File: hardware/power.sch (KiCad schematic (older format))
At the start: 79 parts, among them J100 Conn_01x01, J101 Conn_01x01, J102 Conn_01x01, J39 Screw_Terminal_01x02, J44 Conn_01x01, J45 Conn_01x01, J48 Conn_01x01, J49 Conn_01x01, J50 Conn_01x01, J51 Conn_01x01, J53 Conn_01x01, J54 Conn_01x01, J55 Conn_01x01, J56 Conn_01x01, J57 Conn_01x01, J58 Conn_01x01, J59 Conn_01x01, J68 Conn_01x01, J69 Conn_01x01, J70 Conn_01x01, J94 Conn_01x01, J95 Conn_01x01, J96 Conn_01x01, J98 Conn_01x01, J99 Conn_01x01, Q1 AON6144, U2 LM1117-3.3

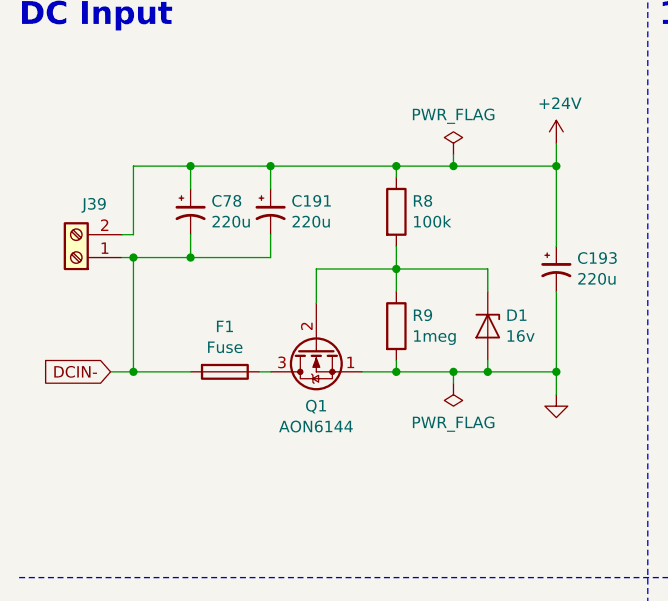
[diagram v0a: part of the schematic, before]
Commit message: replaced stepper driver
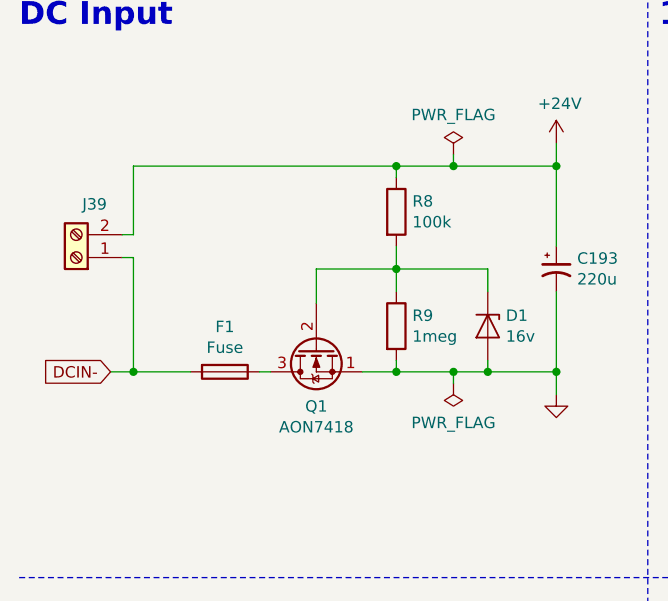
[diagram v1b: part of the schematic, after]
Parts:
- removed C191, C78: 220u, Capacitor_SMD:CP_Elec_6.3x7.7, symbol Device:CP1_Small
- Q1: value AON6144 -> AON7418
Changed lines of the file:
@@
 EESchema Schematic File Version 4
+LIBS:c3dpb-cache
 EELAYER 29 0
 EELAYER END
 $Descr A4 11693 8268
 encoding utf-8
-Sheet 2 10
+Sheet 2 8
 Title "Kajikia - Power Sheet"
 Date "2019-01-23"
@@
 U 1 1 5C3AA6BF
 P 1850 2150
-F 0 "Q1" V 2100 2150 50  0000 C CNN
-F 1 "AON6144" V 2191 2150 50  0000 C CNN
+F 0 "Q1" V 2101 2150 50  0000 C CNN
+F 1 "AON7418" V 2192 2150 50  0000 C CNN
 F 2 "_Generic:DFN5x6-8" H 2050 2250 50  0001 C CNN
 F 3 "~" H 1850 2150 50  0001 C CNN
@@
 	1050 2250 950  2250
 Connection ~ 1050 2250
-Wire Wire Line
-	1050 1350 1300 1350
 $Comp
 L Device:Fuse F1
@@
 	0    1    1    0
 $EndComp
-$Comp
-L Device:CP1_Small C78
-U 1 1 5C8D0CF9
-P 1300 1550
-F 0 "C78" H 1391 1596 50  0000 L CNN
-F 1 "220u" H 1391 1505 50  0000 L CNN
-F 2 "Capacitor_SMD:CP_Elec_6.3x7.7" H 1300 1550 50  0001 C CNN
-F 3 "~" H 1300 1550 50  0001 C CNN
-	1    1300 1550
-	1    0    0    -1
-$EndComp
-Wire Wire Line
-	1300 1650 1300 1750
 Wire Wire Line
 	1050 1750 1050 2250
-$Comp
-L Device:CP1_Small C191
-U 1 1 5C910F5C
-P 1650 1550
-F 0 "C191" H 1741 1596 50  0000 L CNN
-F 1 "220u" H 1741 1505 50  0000 L CNN
-F 2 "Capacitor_SMD:CP_Elec_6.3x7.7" H 1650 1550 50  0001 C CNN
-F 3 "~" H 1650 1550 50  0001 C CNN
-	1    1650 1550
-	1    0    0    -1
-$EndComp
-Wire Wire Line
-	1650 1650 1650 1750
-Wire Wire Line
-	1300 1750 1650 1750
-Connection ~ 1300 1750
 Wire Wire Line
 	1050 1350 1050 1650
-Wire Wire Line
-	1300 1350 1300 1450
-Connection ~ 1300 1350
-Wire Wire Line
-	1300 1350 1650 1350
-Wire Wire Line
-	1650 1350 1650 1450
-Connection ~ 1650 1350
-Wire Wire Line
-	1650 1350 2200 1350
 $Comp
 L Device:CP1_Small C193
@@
 Wire Notes Line
 	550  3150 10100 3150
-Connection ~ 1050 1750
-Wire Wire Line
-	1050 1750 1300 1750
 Wire Wire Line
 	1600 2250 1650 2250
@@
 Text Notes 4450 5350 0    50   ~ 0
 200k - 0.5mhz\n100k - 1mhz\n40k - 2.5mhz
+Wire Wire Line
+	1050 1350 2200 1350
 $EndSCHEMATC

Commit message: layout
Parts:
- F1: footprint _Generic:SMD_Fuseholder -> _Generic:1206_RES
- Q1: footprint _Generic:DFN5x6-8 -> _Generic:DFN3x3A_8L_EP1_P
- U3, U4: renamed from U?; footprint (none) -> Package_TO_SOT_SMD:TSOT-23-8
- gave numbers to parts that had none: 23
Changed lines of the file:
@@
 F 0 "Q1" V 2101 2150 50  0000 C CNN
 F 1 "AON7418" V 2192 2150 50  0000 C CNN
-F 2 "_Generic:DFN5x6-8" H 2050 2250 50  0001 C CNN
+F 2 "_Generic:DFN3x3A_8L_EP1_P" H 2050 2250 50  0001 C CNN
 F 3 "~" H 1850 2150 50  0001 C CNN
 	1    1850 2150
@@
 F 0 "F1" V 1253 2250 50  0000 C CNN
 F 1 "Fuse" V 1344 2250 50  0000 C CNN
-F 2 "_Generic:SMD_Fuseholder" V 1380 2250 50  0001 C CNN
+F 2 "_Generic:1206_RES" V 1380 2250 50  0001 C CNN
 F 3 "~" H 1450 2250 50  0001 C CNN
 	1    1450 2250
@@
 	6600 2100 6350 2100
 $Comp
-L #Regulator:SY8303 U?
+L #Regulator:SY8303 U3
 U 1 1 5D103127
 P 5850 1900
-F 0 "U?" H 6150 2250 50  0000 C CNN
+F 0 "U3" H 6150 2250 50  0000 C CNN
 F 1 "SY8303" H 5600 2250 50  0000 C CNN
-F 2 "" H 5850 1500 50  0001 C CIN
+F 2 "Package_TO_SOT_SMD:TSOT-23-8" H 5850 1500 50  0001 C CIN
 F 3 "" H 5450 2350 50  0001 C CNN
 	1    5850 1900
@@
 	7400 2650 7400 2750
 $Comp
-L Device:C_Small C?
+L Device:C_Small C30
 U 1 1 5D3243B6
 P 8300 1600
-F 0 "C?" H 8392 1691 50  0000 L CNN
+F 0 "C30" H 8392 1691 50  0000 L CNN
 F 1 "22u" H 8392 1600 50  0000 L CNN
 F 2 "_Generic:1210_CAP" H 8300 1600 50  0001 C CNN
@@
 $EndComp
 $Comp
-L Device:C_Small C?
+L Device:C_Small C35
 U 1 1 5D3CAE89
 P 8700 1600
-F 0 "C?" H 8792 1691 50  0000 L CNN
+F 0 "C35" H 8792 1691 50  0000 L CNN
 F 1 "22u" H 8792 1600 50  0000 L CNN
 F 2 "_Generic:1210_CAP" H 8700 1600 50  0001 C CNN
@@
 $EndComp
 $Comp
-L Device:C_Small C?
+L Device:C_Small C41
 U 1 1 5D3CB190
 P 9100 1600
-F 0 "C?" H 9192 1691 50  0000 L CNN
+F 0 "C41" H 9192 1691 50  0000 L CNN
 F 1 "22u" H 9192 1600 50  0000 L CNN
 F 2 "_Generic:1210_CAP" H 9100 1600 50  0001 C CNN
@@
 $EndComp
 $Comp
-L Device:C_Small C?
+L Device:C_Small C32
 U 1 1 5D3CB4A5
 P 8300 2100
-F 0 "C?" H 8392 2191 50  0000 L CNN
+F 0 "C32" H 8392 2191 50  0000 L CNN
 F 1 "22u" H 8392 2100 50  0000 L CNN
 F 2 "_Generic:1210_CAP" H 8300 2100 50  0001 C CNN
@@
 $EndComp
 $Comp
-L Device:C_Small C?
+L Device:C_Small C36
 U 1 1 5D3CBD80
 P 8700 2100
-F 0 "C?" H 8792 2191 50  0000 L CNN
+F 0 "C36" H 8792 2191 50  0000 L CNN
 F 1 "22u" H 8792 2100 50  0000 L CNN
 F 2 "_Generic:1210_CAP" H 8700 2100 50  0001 C CNN
@@
 $EndComp
 $Comp
-L Device:C_Small C?
+L Device:C_Small C42
 U 1 1 5D3CC589
 P 9100 2100
-F 0 "C?" H 9192 2191 50  0000 L CNN
+F 0 "C42" H 9192 2191 50  0000 L CNN
 F 1 "22u" H 9192 2100 50  0000 L CNN
 F 2 "_Generic:1210_CAP" H 9100 2100 50  0001 C CNN
@@
 	8700 2300 9100 2300
 $Comp
-L #Power:GND #PWR?
+L #Power:GND #PWR0111
 U 1 1 5D547413
 P 8700 2450
-F 0 "#PWR?" H 8700 2200 50  0001 C CNN
+F 0 "#PWR0111" H 8700 2200 50  0001 C CNN
 F 1 "GND" H 8700 2300 50  0001 C CNN
 F 2 "" H 8700 2450 50  0001 C CNN
@@
 	4500 2000 4500 1850
 $Comp
-L #Power:GND #PWR?
+L #Power:GND #PWR0125
 U 1 1 5D68CEA0
 P 4500 2000
-F 0 "#PWR?" H 4500 1750 50  0001 C CNN
+F 0 "#PWR0125" H 4500 1750 50  0001 C CNN
 F 1 "GND" H 4500 1850 50  0001 C CNN
 F 2 "" H 4500 2000 50  0001 C CNN
@@
 	4900 1450 4500 1450
 $Comp
-L Device:C_Small C?
+L Device:C_Small C3
 U 1 1 5D63C4F3
 P 4100 1650
-F 0 "C?" H 4192 1741 50  0000 L CNN
+F 0 "C3" H 4192 1741 50  0000 L CNN
 F 1 "4.7u" H 4192 1650 50  0000 L CNN
 F 2 "_Generic:1210_CAP" H 4100 1650 50  0001 C CNN
@@
 $EndComp
 $Comp
-L Device:C_Small C?
+L Device:C_Small C23
 U 1 1 5D63C19E
 P 4500 1650
-F 0 "C?" H 4592 1741 50  0000 L CNN
+F 0 "C23" H 4592 1741 50  0000 L CNN
 F 1 "4.7u" H 4592 1650 50  0000 L CNN
 F 2 "_Generic:1210_CAP" H 4500 1650 50  0001 C CNN
@@
 4.7k - 13.4v\n5.0k - 12.6v\n5.26k - 12.0v
 $Comp
-L Device:C_Small C?
+L Device:C_Small C28
 U 1 1 5D80657C
 P 6600 4250
-F 0 "C?" H 6692 4296 50  0000 L CNN
+F 0 "C28" H 6692 4296 50  0000 L CNN
 F 1 "10n" H 6692 4205 50  0000 L CNN
 F 2 "_Generic:0603_CAP" H 6600 4250 50  0001 C CNN
@@
 	6600 4050 6600 4150
 $Comp
-L Device:R R?
+L Device:R R11
 U 1 1 5D806588
 P 5200 4950
-F 0 "R?" H 5270 4996 50  0000 L CNN
+F 0 "R11" H 5270 4996 50  0000 L CNN
 F 1 "100k" H 5270 4905 50  0000 L CNN
 F 2 "_Generic:0603_RES" V 5130 4950 50  0001 C CNN
@@
 $EndComp
 $Comp
-L Device:L L?
+L Device:L L3
 U 1 1 5D80658E
 P 7150 4500
-F 0 "L?" V 7340 4500 50  0000 C CNN
+F 0 "L3" V 7340 4500 50  0000 C CNN
 F 1 "BCIHP0750-6R8M" V 7249 4500 50  0000 C CNN
 F 2 "_Generic:7x7mm_IND" H 7150 4500 50  0001 C CNN
@@
 Connection ~ 6600 4500
 $Comp
-L Device:R R?
+L Device:R R12
 U 1 1 5D806595
 P 7400 4700
-F 0 "R?" H 7470 4746 50  0000 L CNN
+F 0 "R12" H 7470 4746 50  0000 L CNN
 F 1 "100k" H 7470 4655 50  0000 L CNN
 F 2 "_Generic:0603_RES" V 7330 4700 50  0001 C CNN
@@
 $EndComp
 $Comp
-L Device:R R?
+L Device:R R13
 U 1 1 5D80659B
 P 7400 5100
-F 0 "R?" H 7470 5146 50  0000 L CNN
+F 0 "R13" H 7470 5146 50  0000 L CNN
 F 1 "13.3k" H 7470 5055 50  0000 L CNN
 F 2 "_Generic:0603_RES" V 7330 5100 50  0001 C CNN
@@
 	7400 4500 7300 4500
 $Comp
-L Device:C_Small C?
+L Device:C_Small C29
 U 1 1 5D8065A7
 P 7800 4700
-F 0 "C?" H 7892 4746 50  0000 L CNN
+F 0 "C29" H 7892 4746 50  0000 L CNN
 F 1 "47p" H 7892 4655 50  0000 L CNN
 F 2 "_Generic:0603_CAP" H 7800 4700 50  0001 C CNN
@@
 Connection ~ 7800 4000
 $Comp
-L #Power:GND #PWR?
+L #Power:GND #PWR0126
 U 1 1 5D8065BC
 P 7400 5350
-F 0 "#PWR?" H 7400 5100 50  0001 C CNN
+F 0 "#PWR0126" H 7400 5100 50  0001 C CNN
 F 1 "GND" H 7400 5200 50  0001 C CNN
 F 2 "" H 7400 5350 50  0001 C CNN
@@
 	5850 4050 5850 4100
 $Comp
-L power:PWR_FLAG #FLG?
+L power:PWR_FLAG #FLG0101
 U 1 1 5D8065C3
 P 7800 3850
-F 0 "#FLG?" H 7800 3925 50  0001 C CNN
+F 0 "#FLG0101" H 7800 3925 50  0001 C CNN
 F 1 "PWR_FLAG" H 7800 4024 50  0000 C CNN
 F 2 "" H 7800 3850 50  0001 C CNN
@@
 	5200 5200 5200 5350
 $Comp
-L #Power:GND #PWR?
+L #Power:GND #PWR0127
 U 1 1 5D8065D2
 P 5200 5350
-F 0 "#PWR?" H 5200 5100 50  0001 C CNN
+F 0 "#PWR0127" H 5200 5100 50  0001 C CNN
 F 1 "GND" H 5200 5200 50  0001 C CNN
 F 2 "" H 5200 5350 50  0001 C CNN
@@
 	6600 4700 6350 4700
 $Comp
-L #Regulator:SY8303 U?
+L #Regulator:SY8303 U4
 U 1 1 5D8065DC
 P 5850 4500
-F 0 "U?" H 6150 4850 50  0000 C CNN
+F 0 "U4" H 6150 4850 50  0000 C CNN
 F 1 "SY8303" H 5600 4850 50  0000 C CNN
-F 2 "" H 5850 4100 50  0001 C CIN
+F 2 "Package_TO_SOT_SMD:TSOT-23-8" H 5850 4100 50  0001 C CIN
 F 3 "" H 5450 4950 50  0001 C CNN
 	1    5850 4500
@@
 	7400 5250 7400 5350
 $Comp
-L Device:C_Small C?
+L Device:C_Small C33
 U 1 1 5D8065E5
 P 8300 4200
-F 0 "C?" H 8392 4291 50  0000 L CNN
+F 0 "C33" H 8392 4291 50  0000 L CNN
 F 1 "22u" H 8392 4200 50  0000 L CNN
 F 2 "_Generic:1210_CAP" H 8300 4200 50  0001 C CNN
@@
 $EndComp
 $Comp
-L Device:C_Small C?
+L Device:C_Small C38
 U 1 1 5D8065EC
 P 8700 4200
-F 0 "C?" H 8792 4291 50  0000 L CNN
+F 0 "C38" H 8792 4291 50  0000 L CNN
 F 1 "22u" H 8792 4200 50  0000 L CNN
 F 2 "_Generic:1210_CAP" H 8700 4200 50  0001 C CNN
@@
 $EndComp
 $Comp
-L Device:C_Small C?
+L Device:C_Small C43
 U 1 1 5D8065F3
 P 9100 4200
-F 0 "C?" H 9192 4291 50  0000 L CNN
+F 0 "C43" H 9192 4291 50  0000 L CNN
 F 1 "22u" H 9192 4200 50  0000 L CNN
 F 2 "_Generic:1210_CAP" H 9100 4200 50  0001 C CNN
@@
 $EndComp
 $Comp
-L Device:C_Small C?
+L Device:C_Small C34
 U 1 1 5D8065FA
 P 8300 4700
-F 0 "C?" H 8392 4791 50  0000 L CNN
+F 0 "C34" H 8392 4791 50  0000 L CNN
 F 1 "22u" H 8392 4700 50  0000 L CNN
 F 2 "_Generic:1210_CAP" H 8300 4700 50  0001 C CNN
@@
 $EndComp
 $Comp
-L Device:C_Small C?
+L Device:C_Small C40
 U 1 1 5D806601
 P 8700 4700
-F 0 "C?" H 8792 4791 50  0000 L CNN
+F 0 "C40" H 8792 4791 50  0000 L CNN
 F 1 "22u" H 8792 4700 50  0000 L CNN
 F 2 "_Generic:1210_CAP" H 8700 4700 50  0001 C CNN
@@
 $EndComp
 $Comp
-L Device:C_Small C?
+L Device:C_Small C44
 U 1 1 5D806608
 P 9100 4700
-F 0 "C?" H 9192 4791 50  0000 L CNN
+F 0 "C44" H 9192 4791 50  0000 L CNN
 F 1 "22u" H 9192 4700 50  0000 L CNN
 F 2 "_Generic:1210_CAP" H 9100 4700 50  0001 C CNN
@@
 	8700 4900 9100 4900
 $Comp
-L #Power:GND #PWR?
+L #Power:GND #PWR0128
 U 1 1 5D806629
 P 8700 5050
-F 0 "#PWR?" H 8700 4800 50  0001 C CNN
+F 0 "#PWR0128" H 8700 4800 50  0001 C CNN
 F 1 "GND" H 8700 4900 50  0001 C CNN
 F 2 "" H 8700 5050 50  0001 C CNN
@@
 	4500 4600 4500 4450
 $Comp
-L #Power:GND #PWR?
+L #Power:GND #PWR0129
 U 1 1 5D806637
 P 4500 4600
-F 0 "#PWR?" H 4500 4350 50  0001 C CNN
+F 0 "#PWR0129" H 4500 4350 50  0001 C CNN
 F 1 "GND" H 4500 4450 50  0001 C CNN
 F 2 "" H 4500 4600 50  0001 C CNN
@@
 	4900 4050 4500 4050
 $Comp
-L Device:C_Small C?
+L Device:C_Small C5
 U 1 1 5D80664A
 P 4100 4250
-F 0 "C?" H 4192 4341 50  0000 L CNN
+F 0 "C5" H 4192 4341 50  0000 L CNN
 F 1 "4.7u" H 4192 4250 50  0000 L CNN
 F 2 "_Generic:1210_CAP" H 4100 4250 50  0001 C CNN
@@
 $EndComp
 $Comp
-L Device:C_Small C?
+L Device:C_Small C24
 U 1 1 5D806651
 P 4500 4250
-F 0 "C?" H 4592 4341 50  0000 L CNN
+F 0 "C24" H 4592 4341 50  0000 L CNN
 F 1 "4.7u" H 4592 4250 50  0000 L CNN
 F 2 "_Generic:1210_CAP" H 4500 4250 50  0001 C CNN
@@
 	4900 4050 4900 4150
 $Comp
-L power:+24V #PWR?
+L power:+24V #PWR0130
 U 1 1 5D806659
 P 4500 3900
-F 0 "#PWR?" H 4500 3750 50  0001 C CNN
+F 0 "#PWR0130" H 4500 3750 50  0001 C CNN
 F 1 "+24V" H 4515 4073 50  0000 C CNN
 F 2 "" H 4500 3900 50  0001 C CNN
@@
 $EndComp
 $Comp
-L Device:C_Small C?
+L Device:C_Small C25
 U 1 1 5D806660
 P 4900 4250
-F 0 "C?" H 4992 4341 50  0000 L CNN
+F 0 "C25" H 4992 4341 50  0000 L CNN
 F 1 "4.7u" H 4992 4250 50  0000 L CNN
 F 2 "_Generic:1210_CAP" H 4900 4250 50  0001 C CNN
@@
 13.0k - 5.22v\n13.3k - 5.11v\n13.64k - 5.0v
 $Comp
-L power:+5V #PWR?
+L power:+5V #PWR0131
 U 1 1 5D82065F
 P 8700 3850
-F 0 "#PWR?" H 8700 3700 50  0001 C CNN
+F 0 "#PWR0131" H 8700 3700 50  0001 C CNN
 F 1 "+5V" H 8715 4023 50  0000 C CNN
 F 2 "" H 8700 3850 50  0001 C CNN

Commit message: power reg
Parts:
- C3, C5: value 4.7u -> 100n; footprint _Generic:1210_CAP -> _Generic:0603_CAP; Voltage 35v -> (none)
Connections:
- net GND: now also C30.2, C33.2, C35.2, C38.2, C41.2, C43.2
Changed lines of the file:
@@
 	4900 1450 4500 1450
-$Comp
-L Device:C_Small C3
-U 1 1 5D63C4F3
-P 4100 1650
-F 0 "C3" H 4192 1741 50  0000 L CNN
-F 1 "4.7u" H 4192 1650 50  0000 L CNN
-F 2 "_Generic:1210_CAP" H 4100 1650 50  0001 C CNN
-F 3 "~" H 4100 1650 50  0001 C CNN
-F 4 "35v" H 4192 1559 50  0000 L CNN "Voltage"
-	1    4100 1650
-	1    0    0    -1
-$EndComp
 $Comp
 L Device:C_Small C23
@@
 	4900 4050 4500 4050
 $Comp
-L Device:C_Small C5
-U 1 1 5D80664A
-P 4100 4250
-F 0 "C5" H 4192 4341 50  0000 L CNN
-F 1 "4.7u" H 4192 4250 50  0000 L CNN
-F 2 "_Generic:1210_CAP" H 4100 4250 50  0001 C CNN
-F 3 "~" H 4100 4250 50  0001 C CNN
-F 4 "35v" H 4192 4159 50  0000 L CNN "Voltage"
-	1    4100 4250
-	1    0    0    -1
-$EndComp
-$Comp
 L Device:C_Small C24
 U 1 1 5D806651
@@
 Wire Wire Line
 	1050 1350 2200 1350
+Wire Wire Line
+	8300 1800 8150 1800
+Wire Wire Line
+	8150 1800 8150 2300
+Wire Wire Line
+	8150 2300 8300 2300
+Connection ~ 8300 1800
+Connection ~ 8300 2300
+$Comp
+L Device:C_Small C3
+U 1 1 5D28B4FF
+P 4100 1650
+F 0 "C3" H 4192 1696 50  0000 L CNN
+F 1 "100n" H 4192 1605 50  0000 L CNN
+F 2 "_Generic:0603_CAP" H 4100 1650 50  0001 C CNN
+F 3 "~" H 4100 1650 50  0001 C CNN
+	1    4100 1650
+	1    0    0    -1
+$EndComp
+$Comp
+L Device:C_Small C5
+U 1 1 5D29C329
+P 4100 4250
+F 0 "C5" H 4192 4296 50  0000 L CNN
+F 1 "100n" H 4192 4205 50  0000 L CNN
+F 2 "_Generic:0603_CAP" H 4100 4250 50  0001 C CNN
+F 3 "~" H 4100 4250 50  0001 C CNN
+	1    4100 4250
+	1    0    0    -1
+$EndComp
+Wire Wire Line
+	8300 4900 8150 4900
+Wire Wire Line
+	8150 4900 8150 4400
+Wire Wire Line
+	8150 4400 8300 4400
+Connection ~ 8300 4900
+Connection ~ 8300 4400
 $EndSCHEMATC

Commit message: combine
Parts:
- removed H5, H6: MountingHole, MountingHole:MountingHole_2.2mm_M2_DIN965, symbol Mechanical:MountingHole
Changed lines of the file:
@@
 	10500 3600 10500 3750
 Connection ~ 10500 3450
-$Comp
-L Mechanical:MountingHole H5
-U 1 1 5C4CA30F
-P 1700 3800
-F 0 "H5" H 1800 3846 50  0000 L CNN
-F 1 "MountingHole" H 1800 3755 50  0000 L CNN
-F 2 "MountingHole:MountingHole_2.2mm_M2_DIN965" H 1700 3800 50  0001 C CNN
-F 3 "~" H 1700 3800 50  0001 C CNN
-	1    1700 3800
-	1    0    0    -1
-$EndComp
-$Comp
-L Mechanical:MountingHole H6
-U 1 1 5C4CA407
-P 1700 4050
-F 0 "H6" H 1800 4096 50  0000 L CNN
-F 1 "MountingHole" H 1800 4005 50  0000 L CNN
-F 2 "MountingHole:MountingHole_2.2mm_M2_DIN965" H 1700 4050 50  0001 C CNN
-F 3 "~" H 1700 4050 50  0001 C CNN
-	1    1700 4050
-	1    0    0    -1
-$EndComp
 Wire Wire Line
 	10500 4350 10500 4500

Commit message: routing
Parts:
- added C53: 220u, Capacitor_SMD:CP_Elec_6.3x7.7, symbol Device:CP1_Small
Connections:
- net +24V: now also C53.1
- net GND: now also C53.2
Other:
- moved on the sheet: C193, D1, F1, Q1, R8, R9
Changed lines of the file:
@@
 Power LED
 Wire Wire Line
-	1050 2250 1300 2250
+	1050 2250 1100 2250
 $Comp
 L Device:Q_NMOS_SGD Q1
 U 1 1 5C3AA6BF
-P 1850 2150
-F 0 "Q1" V 2101 2150 50  0000 C CNN
-F 1 "AON7418" V 2192 2150 50  0000 C CNN
-F 2 "_Generic:DFN3x3A_8L_EP1_P" H 2050 2250 50  0001 C CNN
-F 3 "~" H 1850 2150 50  0001 C CNN
-	1    1850 2150
+P 1650 2150
+F 0 "Q1" V 1901 2150 50  0000 C CNN
+F 1 "AON7418" V 1992 2150 50  0000 C CNN
+F 2 "_Generic:DFN3x3A_8L_EP1_P" H 1850 2250 50  0001 C CNN
+F 3 "~" H 1650 2150 50  0001 C CNN
+	1    1650 2150
 	0    -1   1    0
 $EndComp
 Wire Wire Line
-	2050 2250 2200 2250
+	1850 2250 2000 2250
 $Comp
 L Device:R R8
 U 1 1 5C407302
-P 2200 1550
-F 0 "R8" H 2270 1596 50  0000 L CNN
-F 1 "100k" H 2270 1505 50  0000 L CNN
-F 2 "_Generic:0603_RES" V 2130 1550 50  0001 C CNN
-F 3 "~" H 2200 1550 50  0001 C CNN
-	1    2200 1550
+P 2000 1550
+F 0 "R8" H 2070 1596 50  0000 L CNN
+F 1 "100k" H 2070 1505 50  0000 L CNN
+F 2 "_Generic:0603_RES" V 1930 1550 50  0001 C CNN
+F 3 "~" H 2000 1550 50  0001 C CNN
+	1    2000 1550
 	1    0    0    -1
 $EndComp
@@
 L Device:D_Zener D1
 U 1 1 5C407892
-P 2600 2050
-F 0 "D1" V 2554 2129 50  0000 L CNN
-F 1 "16v" V 2645 2129 50  0000 L CNN
-F 2 "_Generic:SOD-523_DIODE" H 2600 2050 50  0001 C CNN
-F 3 "~" H 2600 2050 50  0001 C CNN
-	1    2600 2050
+P 2400 2050
+F 0 "D1" V 2354 2129 50  0000 L CNN
+F 1 "16v" V 2445 2129 50  0000 L CNN
+F 2 "_Generic:SOD-523_DIODE" H 2400 2050 50  0001 C CNN
+F 3 "~" H 2400 2050 50  0001 C CNN
+	1    2400 2050
 	0    1    1    0
 $EndComp
 Wire Wire Line
-	2600 1900 2600 1800
-Wire Wire Line
-	2600 1800 2200 1800
-Wire Wire Line
-	1850 1800 1850 1950
-Wire Wire Line
-	2200 1800 2200 1700
-Wire Wire Line
-	2600 2200 2600 2250
-Connection ~ 2600 2250
+	2400 1900 2400 1800
+Wire Wire Line
+	2400 1800 2000 1800
+Wire Wire Line
+	1650 1800 1650 1950
+Wire Wire Line
+	2000 1800 2000 1700
+Wire Wire Line
+	2400 2200 2400 2250
+Connection ~ 2400 2250
 $Comp
 L Device:R R9
 U 1 1 5C479547
-P 2200 2050
-F 0 "R9" H 2270 2096 50  0000 L CNN
-F 1 "1meg" H 2270 2005 50  0000 L CNN
-F 2 "_Generic:0603_RES" V 2130 2050 50  0001 C CNN
-F 3 "~" H 2200 2050 50  0001 C CNN
-	1    2200 2050
-	1    0    0    -1
-$EndComp
-Wire Wire Line
-	2200 2200 2200 2250
-Connection ~ 2200 2250
-Wire Wire Line
-	2200 1900 2200 1800
-Connection ~ 2200 1800
-Wire Wire Line
-	2200 1800 1850 1800
+P 2000 2050
+F 0 "R9" H 2070 2096 50  0000 L CNN
+F 1 "1meg" H 2070 2005 50  0000 L CNN
+F 2 "_Generic:0603_RES" V 1930 2050 50  0001 C CNN
+F 3 "~" H 2000 2050 50  0001 C CNN
+	1    2000 2050
+	1    0    0    -1
+$EndComp
+Wire Wire Line
+	2000 2200 2000 2250
+Connection ~ 2000 2250
+Wire Wire Line
+	2000 1900 2000 1800
+Connection ~ 2000 1800
+Wire Wire Line
+	2000 1800 1650 1800
 $Comp
 L power:PWR_FLAG #FLG07
 U 1 1 5C5382D5
-P 2450 2300
-F 0 "#FLG07" H 2450 2375 50  0001 C CNN
-F 1 "PWR_FLAG" H 2450 2473 50  0000 C CNN
-F 2 "" H 2450 2300 50  0001 C CNN
-F 3 "~" H 2450 2300 50  0001 C CNN
-	1    2450 2300
+P 2250 2300
+F 0 "#FLG07" H 2250 2375 50  0001 C CNN
+F 1 "PWR_FLAG" H 2250 2473 50  0000 C CNN
+F 2 "" H 2250 2300 50  0001 C CNN
+F 3 "~" H 2250 2300 50  0001 C CNN
+	1    2250 2300
 	-1   0    0    1
 $EndComp
 Wire Wire Line
-	2450 2300 2450 2250
+	2250 2300 2250 2250
 $Comp
 L power:PWR_FLAG #FLG06
@@
 	2450 1300 2450 1350
 Wire Wire Line
-	2200 1400 2200 1350
-Connection ~ 2200 1350
+	2000 1400 2000 1350
+Connection ~ 2000 1350
 $Comp
 L Connector:Screw_Terminal_01x02 J39
@@
 L Device:Fuse F1
 U 1 1 5C420B0B
-P 1450 2250
-F 0 "F1" V 1253 2250 50  0000 C CNN
-F 1 "Fuse" V 1344 2250 50  0000 C CNN
-F 2 "_Generic:1206_RES" V 1380 2250 50  0001 C CNN
-F 3 "~" H 1450 2250 50  0001 C CNN
-	1    1450 2250
+P 1250 2250
+F 0 "F1" V 1053 2250 50  0000 C CNN
+F 1 "Fuse" V 1144 2250 50  0000 C CNN
+F 2 "_Generic:1206_RES" V 1180 2250 50  0001 C CNN
+F 3 "~" H 1250 2250 50  0001 C CNN
+	1    1250 2250
 	0    1    1    0
 $EndComp
@@
 L Device:CP1_Small C193
 U 1 1 5C426A5B
-P 2900 1800
-F 0 "C193" H 2991 1846 50  0000 L CNN
-F 1 "220u" H 2991 1755 50  0000 L CNN
-F 2 "Capacitor_SMD:CP_Elec_6.3x7.7" H 2900 1800 50  0001 C CNN
-F 3 "~" H 2900 1800 50  0001 C CNN
-	1    2900 1800
+P 2650 1800
+F 0 "C193" H 2741 1846 50  0000 L CNN
+F 1 "220u" H 2741 1755 50  0000 L CNN
+F 2 "Capacitor_SMD:CP_Elec_6.3x7.7" H 2650 1800 50  0001 C CNN
+F 3 "~" H 2650 1800 50  0001 C CNN
+	1    2650 1800
 	1    0    0    -1
 $EndComp
@@
 	550  3150 10100 3150
 Wire Wire Line
-	1600 2250 1650 2250
-Wire Wire Line
-	2900 1900 2900 2250
-Wire Wire Line
-	2900 2250 2600 2250
-Wire Wire Line
-	2900 1350 2900 1700
-Connection ~ 2900 1350
-Wire Wire Line
-	2200 1350 2450 1350
-Connection ~ 2900 2250
+	1400 2250 1450 2250
+Wire Wire Line
+	2650 1900 2650 2250
+Wire Wire Line
+	2900 2250 2650 2250
+Wire Wire Line
+	2650 1350 2650 1700
+Wire Wire Line
+	2000 1350 2450 1350
 Connection ~ 2450 1350
 Wire Wire Line
-	2450 1350 2900 1350
-Connection ~ 2450 2250
-Wire Wire Line
-	2450 2250 2600 2250
-Wire Wire Line
-	2200 2250 2450 2250
+	2450 1350 2650 1350
+Connection ~ 2250 2250
+Wire Wire Line
+	2250 2250 2400 2250
+Wire Wire Line
+	2000 2250 2250 2250
 Wire Wire Line
 	5350 1700 5300 1700
@@
 200k - 0.5mhz\n100k - 1mhz\n40k - 2.5mhz
 Wire Wire Line
-	1050 1350 2200 1350
+	1050 1350 2000 1350
 Wire Wire Line
 	8300 1800 8150 1800
@@
 Connection ~ 8300 4900
 Connection ~ 8300 4400
+Connection ~ 2650 1350
+Wire Wire Line
+	2650 1350 2900 1350
+Connection ~ 2650 2250
+Wire Wire Line
+	2650 2250 2400 2250
+$Comp
+L Device:CP1_Small C53
+U 1 1 5D443E9E
+P 3050 1800
+F 0 "C53" H 3141 1846 50  0000 L CNN
+F 1 "220u" H 3141 1755 50  0000 L CNN
+F 2 "Capacitor_SMD:CP_Elec_6.3x7.7" H 3050 1800 50  0001 C CNN
+F 3 "~" H 3050 1800 50  0001 C CNN
+	1    3050 1800
+	1    0    0    -1
+$EndComp
+Wire Wire Line
+	3050 1900 3050 2250
+Wire Wire Line
+	3050 1350 3050 1700
+Wire Wire Line
+	3050 1350 2900 1350
+Connection ~ 2900 1350
+Wire Wire Line
+	3050 2250 2900 2250
+Connection ~ 2900 2250
 $EndSCHEMATC
